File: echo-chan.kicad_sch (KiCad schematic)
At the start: 50 parts, among them J1 SJ1-3533NS, J2 USB_B, SW1 SW_Push, T1 Transformer_1P_1S, U1 JAMMA, U2 JAMMA, U3 AT90USB1286, U4 HD15, U6 THS7374, Y1 16MHz

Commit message: [SCHEMATIC] assign footprints to symbols
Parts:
- C11, C3, C8: footprint (none) -> Capacitor_SMD:C_0805_2012Metric
- C15, C17, C19, C21: footprint (none) -> Capacitor_THT:CP_Radial_D8.0mm_P3.50mm
- J2: footprint footprints:USB_B_OST_USB-B1HSxx_Horizontal -> Connector_USB:USB_B_OST_USB-B1HSxx_Horizontal
- R1, R10, R11, R12, R13, R14, R15, R16, R17, R2, R3, R4, R40, R5, R6, R7, R8, R9: footprint footprints:R_0805_2012Metric -> Resistor_SMD:R_0805_2012Metric
- SW1: footprint footprints:BUTTON -> Button_Switch_THT:SW_PUSH_6mm
- U3: footprint footprints:TQFP-64_14x14mm_P0.8mm -> Package_QFP:TQFP-64_14x14mm_P0.8mm
- U4: footprint footprints:DSUB-15-HD_Female_Horizontal_P2.29x2.54mm_EdgePinOffset9.40mm -> Connector_Dsub:DSUB-15-HD_Female_Horizontal_P2.29x2.54mm_EdgePinOffset9.40mm
- Y1: footprint footprints:Crystal_SMD_SeikoEpson_FA238-4Pin_3.2x2.5mm -> Crystal:Crystal_HC49-4H_Vertical
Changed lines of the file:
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@@
 			)
 		)
-		(property "Footprint" "footprints:TQFP-64_14x14mm_P0.8mm"
+		(property "Footprint" "Package_QFP:TQFP-64_14x14mm_P0.8mm"
 			(at 209.55 69.85 0)
 			(effects
@@
 			)
 		)
-		(property "Footprint" "footprints:R_0805_2012Metric"
+		(property "Footprint" "Resistor_SMD:R_0805_2012Metric"
 			(at 137.16 106.172 90)
 			(effects
@@
 			)
 		)
-		(property "Footprint" "footprints:R_0805_2012Metric"
+		(property "Footprint" "Resistor_SMD:R_0805_2012Metric"
 			(at 137.16 108.712 90)
 			(effects
@@
 			)
 		)
-		(property "Footprint" "footprints:R_0805_2012Metric"
+		(property "Footprint" "Resistor_SMD:R_0805_2012Metric"
 			(at 269.24 69.342 90)
 			(effects
@@
 			)
 		)
-		(property "Footprint" "footprints:BUTTON"
+		(property "Footprint" "Button_Switch_THT:SW_PUSH_6mm"
 			(at 207.01 120.65 0)
 			(effects
@@
 			)
 		)
-		(property "Footprint" "footprints:Crystal_SMD_SeikoEpson_FA238-4Pin_3.2x2.5mm"
+		(property "Footprint" "Crystal:Crystal_HC49-4H_Vertical"
 			(at 236.22 119.38 0)
 			(effects
@@
 			)
 		)
-		(property "Footprint" "footprints:DSUB-15-HD_Female_Horizontal_P2.29x2.54mm_EdgePinOffset9.40mm"
+		(property "Footprint" "Connector_Dsub:DSUB-15-HD_Female_Horizontal_P2.29x2.54mm_EdgePinOffset9.40mm"
 			(at 128.27 33.02 0)
 			(effects
@@
 			)
 		)
-		(property "Footprint" "footprints:USB_B_OST_USB-B1HSxx_Horizontal"
+		(property "Footprint" "Connector_USB:USB_B_OST_USB-B1HSxx_Horizontal"
 			(at 129.54 109.22 0)
 			(effects
@@
 		(on_board yes)
 		(dnp no)
-		(property "Reference" "#PWR?"
+		(property "Reference" "#PWR0101"
 			(at 240.03 165.1 0)
 			(effects
@@
 			(project "echo-chan"
 				(path "/f9e5ab77-ac00-48f5-910f-38a287c63fee"
-					(reference "#PWR?")
+					(reference "#PWR0101")
 					(unit 1)
 				)
@@
 			)
 		)
-		(property "Footprint" "footprints:R_0805_2012Metric"
+		(property "Footprint" "Resistor_SMD:R_0805_2012Metric"
 			(at 209.55 150.368 90)
 			(effects
@@
 			)
 		)
-		(property "Footprint" "footprints:R_0805_2012Metric"
+		(property "Footprint" "Resistor_SMD:R_0805_2012Metric"
 			(at 209.55 160.528 90)
 			(effects
@@
 			)
 		)
-		(property "Footprint" "footprints:R_0805_2012Metric"
+		(property "Footprint" "Resistor_SMD:R_0805_2012Metric"
 			(at 212.852 153.67 90)
 			(effects
@@
 			)
 		)
-		(property "Footprint" ""
+		(property "Footprint" "Capacitor_THT:CP_Radial_D8.0mm_P3.50mm"
 			(at 120.65 176.53 0)
 			(effects
@@
 			)
 		)
-		(property "Footprint" ""
+		(property "Footprint" "Capacitor_THT:CP_Radial_D8.0mm_P3.50mm"
 			(at 120.65 185.42 0)
 			(effects
@@
 			)
 		)
-		(property "Footprint" ""
+		(property "Footprint" "Capacitor_SMD:C_0805_2012Metric"
 			(at 245.11 115.57 0)
 			(effects
@@
 			)
 		)
-		(property "Footprint" "footprints:R_0805_2012Metric"
+		(property "Footprint" "Resistor_SMD:R_0805_2012Metric"
 			(at 40.64 162.052 90)
 			(effects
@@
 			)
 		)
-		(property "Footprint" ""
+		(property "Footprint" "Capacitor_THT:CP_Radial_D8.0mm_P3.50mm"
 			(at 120.65 158.75 0)
 			(effects
@@
 			)
 		)
-		(property "Footprint" "footprints:R_0805_2012Metric"
+		(property "Footprint" "Resistor_SMD:R_0805_2012Metric"
 			(at 45.212 181.61 90)
 			(effects
@@
 			)
 		)
-		(property "Footprint" "footprints:R_0805_2012Metric"
+		(property "Footprint" "Resistor_SMD:R_0805_2012Metric"
 			(at 57.912 181.61 90)
 			(effects
@@
 			)
 		)
-		(property "Footprint" ""
+		(property "Footprint" "Capacitor_SMD:C_0805_2012Metric"
 			(at 184.15 73.66 0)
 			(effects
@@
 			)
 		)
-		(property "Footprint" ""
+		(property "Footprint" "Capacitor_SMD:C_0805_2012Metric"
 			(at 245.11 123.19 0)
 			(effects
@@
 			)
 		)
-		(property "Footprint" "footprints:R_0805_2012Metric"
+		(property "Footprint" "Resistor_SMD:R_0805_2012Metric"
 			(at 104.14 169.672 90)
 			(effects
@@
 			)
 		)
-		(property "Footprint" "footprints:R_0805_2012Metric"
+		(property "Footprint" "Resistor_SMD:R_0805_2012Metric"
 			(at 104.14 162.052 90)
 			(effects
@@
 			)
 		)
-		(property "Footprint" "footprints:R_0805_2012Metric"
+		(property "Footprint" "Resistor_SMD:R_0805_2012Metric"
 			(at 40.64 164.592 90)
 			(effects
@@
 			)
 		)
-		(property "Footprint" ""
+		(property "Footprint" "Capacitor_THT:CP_Radial_D8.0mm_P3.50mm"
 			(at 120.65 167.64 0)
 			(effects
@@
 			)
 		)
-		(property "Footprint" "footprints:R_0805_2012Metric"
+		(property "Footprint" "Resistor_SMD:R_0805_2012Metric"
 			(at 40.64 169.672 90)
 			(effects
@@
 			)
 		)
-		(property "Footprint" "footprints:R_0805_2012Metric"
+		(property "Footprint" "Resistor_SMD:R_0805_2012Metric"
 			(at 40.64 167.132 90)
 			(effects
@@
 			)
 		)
-		(property "Footprint" "footprints:R_0805_2012Metric"
+		(property "Footprint" "Resistor_SMD:R_0805_2012Metric"
 			(at 64.262 181.61 90)
 			(effects
@@
 			)
 		)
-		(property "Footprint" "footprints:R_0805_2012Metric"
+		(property "Footprint" "Resistor_SMD:R_0805_2012Metric"
 			(at 104.14 167.132 90)
 			(effects
@@
 			)
 		)
-		(property "Footprint" "footprints:R_0805_2012Metric"
+		(property "Footprint" "Resistor_SMD:R_0805_2012Metric"
 			(at 51.562 181.61 90)
 			(effects
@@
 			)
 		)
-		(property "Footprint" "footprints:R_0805_2012Metric"
+		(property "Footprint" "Resistor_SMD:R_0805_2012Metric"
 			(at 104.14 164.592 90)
 			(effects

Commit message: [SCHEMATIC] Change +5V to VBUS for MCU
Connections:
- net +5V: no longer C1.1, C2.1, C4.1, C7.1, C9.2, J2.1 (VBUS), U3.21 (VCC), U3.3 (UVcc), U3.52 (VCC), U3.64 (AVCC), U3.8 (VBus)
- new net VBUS: C1.1, C2.1, C4.1, C7.1, C9.2, J2.1 (VBUS), U3.21 (VCC), U3.3 (UVcc), U3.52 (VCC), U3.64 (AVCC), U3.8 (VBus)
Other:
- moved on the sheet: C2, C5, C7, C9

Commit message: [SCHEMATIC] Fix typos in schematic block labels
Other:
- note added: "AUDIO OUT"
- note added: "MICROCONTROLLER"
- note removed: "AUDIO TRANSFORMER"
- note removed: "MICRCONTROLLER"
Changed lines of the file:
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@@
 		)
 	)
-	(text "MICRCONTROLLER"
+	(text "MICROCONTROLLER"
 		(exclude_from_sim no)
 		(at 226.06 15.748 0)
@@
 		)
 	)
-	(text "AUDIO TRANSFORMER"
+	(text "AUDIO OUT"
 		(exclude_from_sim no)
 		(at 227.076 139.7 0)

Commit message: [SCHEMATIC] Fix inverted U2 JAMMA edge
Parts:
- U4: footprint Connector_Dsub:DSUB-15-HD_Female_Horizontal_P2.29x2.54mm_EdgePinOffset9.40mm -> echo-chan:DSUB-15-HD_Female_Horizontal_P2.29x2.54mm_EdgePinOffset9.40mm_anchors
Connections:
- net +12V: now also U2.6 (+12V), U2.F (+12V); no longer U2.23 (P1_BUTTON_2), U2.a (P2_BUTTON_2)
- net +5V: now also U2.3 (+5V), U2.4 (+5V), U2.C (+5V), U2.D (+5V); no longer U2.25 (P1_BUTTON_4), U2.26 (P1_BUTTON_5), U2.c (P2_BUTTON_4), U2.d (P2_BUTTON_5)
- net -5V: now also U2.5 (-5V), U2.E (-5V); no longer U2.24 (P1_BUTTON_3), U2.b (P2_BUTTON_3)
- net COIN_1: now also U2.16 (COIN_1); no longer U2.P (VIDEO_SYNC)
- net COIN_2: now also U2.T (COIN_2); no longer U2.13 (VIDEO_BLUE)
- net COIN_COUNT_1: now also U2.8 (COIN_COUNTER_1); no longer U2.Y (P2_RIGHT)
- net COIN_COUNT_2: now also U2.J (COIN_COUNTER_2); no longer U2.21 (P1_RIGHT)
- net COIN_LOCK_1: now also U2.9 (COIN_LOCKOUT_1); no longer U2.X (P2_LEFT)
- net COIN_LOCK_2: now also U2.K (COIN_LOCKOUT_2); no longer U2.20 (P1_LEFT)
- net P1_B1: now also U2.22 (P1_BUTTON_1); no longer U2.H (KEY)
- net P1_B2: now also U2.23 (P1_BUTTON_2); no longer U2.F (+12V)
- net P1_B3: now also U2.24 (P1_BUTTON_3); no longer U2.E (-5V)
- net P1_B4: now also U2.25 (P1_BUTTON_4); no longer U2.D (+5V)
- net P1_B5: now also U2.26 (P1_BUTTON_5); no longer U2.C (+5V)
- net P1_DOWN: now also U2.19 (P1_DOWN); no longer U2.L (SPEAKER(-))
- net P1_LEFT: now also U2.20 (P1_LEFT); no longer U2.K (COIN_LOCKOUT_2)
- net P1_RIGHT: now also U2.21 (P1_RIGHT); no longer U2.J (COIN_COUNTER_2)
- net P1_START: now also U2.17 (P1_START); no longer U2.N (VIDEO_GREEN)
- net P1_UP: now also U2.18 (P1_UP); no longer U2.M (NC)
- net P2_B1: now also U2.Z (P2_BUTTON_1); no longer U2.7 (KEY)
- net P2_B2: now also U2.a (P2_BUTTON_2); no longer U2.6 (+12V)
- net P2_B3: now also U2.b (P2_BUTTON_3); no longer U2.5 (-5V)
- net P2_B4: now also U2.c (P2_BUTTON_4); no longer U2.4 (+5V)
- net P2_B5: now also U2.d (P2_BUTTON_5); no longer U2.3 (+5V)
- net P2_DOWN: now also U2.W (P2_DOWN); no longer U2.10 (SPEAKER(+))
- net P2_LEFT: now also U2.X (P2_LEFT); no longer U2.9 (COIN_LOCKOUT_1)
- net P2_RIGHT: now also U2.Y (P2_RIGHT); no longer U2.8 (COIN_COUNTER_1)
- net P2_START: now also U2.U (P2_START); no longer U2.12 (VIDEO_RED)
- net P2_UP: now also U2.V (P2_UP); no longer U2.11 (NC)
- net SERVICE: now also U2.R (SERVICE); no longer U2.15 (TEST)
- net SPEAKER+: now also U2.10 (SPEAKER(+)); no longer U2.W (P2_DOWN)
- net SPEAKER-: now also U2.L (SPEAKER(-)); no longer U2.19 (P1_DOWN)
- net TEST: now also U2.15 (TEST); no longer U2.R (SERVICE)
- net TILT: now also U2.S (TILT); no longer U2.14 (VIDEO_GND)
- net VIDEO_BLUE: now also U2.13 (VIDEO_BLUE); no longer U2.T (COIN_2)
- net VIDEO_GND: now also U2.14 (VIDEO_GND); no longer U2.S (TILT)
- net VIDEO_GREEN: now also U2.N (VIDEO_GREEN); no longer U2.17 (P1_START)
- net VIDEO_RED: now also U2.12 (VIDEO_RED); no longer U2.U (P2_START)
- net VIDEO_SYNC: now also U2.P (VIDEO_SYNC); no longer U2.16 (COIN_1)
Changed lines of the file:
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@@
 	)
 	(junction
+		(at 73.66 27.94)
+		(diameter 0)
+		(color 0 0 0 0)
+	)
+	(junction
 		(at 214.63 148.59)
 		(diameter 0)
@@
 	)
 	(junction
-		(at 73.66 27.94)
-		(diameter 0)
-		(color 0 0 0 0)
-	)
-	(junction
 		(at 39.37 29.21)
 		(diameter 0)
@@
 	(symbol
 		(lib_id "jamma-streamer-rescue:JAMMA-jamma-streamer-rescue")
-		(at 66.04 63.5 270)
-		(mirror x)
+		(at 66.04 62.23 270)
 		(unit 1)
 		(exclude_from_sim no)
@@
 		(dnp no)
 		(property "Reference" "U2"
-			(at 58.42 63.5 0)
+			(at 63.754 25.4 90)
 			(effects
 				(font
@@
 		)
 		(property "Value" "JAMMA"
-			(at 60.96 63.5 0)
+			(at 60.96 62.23 0)
 			(effects
 				(font
@@
 		)
 		(property "Footprint" "footprints:JAMMA"
-			(at 63.5 71.12 0)
+			(at 63.5 54.61 0)
 			(effects
 				(font
@@
 		)
 		(property "Datasheet" ""
-			(at 63.5 71.12 0)
+			(at 63.5 54.61 0)
 			(effects
 				(font
@@
 		)
 		(property "Description" ""
-			(at 66.04 63.5 0)
+			(at 66.04 62.23 0)
 			(effects
 				(font
@@
 		(dnp no)
 		(property "Reference" "U1"
-			(at 24.13 62.23 0)
+			(at 29.718 25.4 90)
 			(effects
 				(font
@@
 			)
 		)
-		(property "Footprint" "Connector_Dsub:DSUB-15-HD_Female_Horizontal_P2.29x2.54mm_EdgePinOffset9.40mm"
+		(property "Footprint" "echo-chan:DSUB-15-HD_Female_Horizontal_P2.29x2.54mm_EdgePinOffset9.40mm_anchors"
 			(at 128.27 33.02 0)
 			(effects

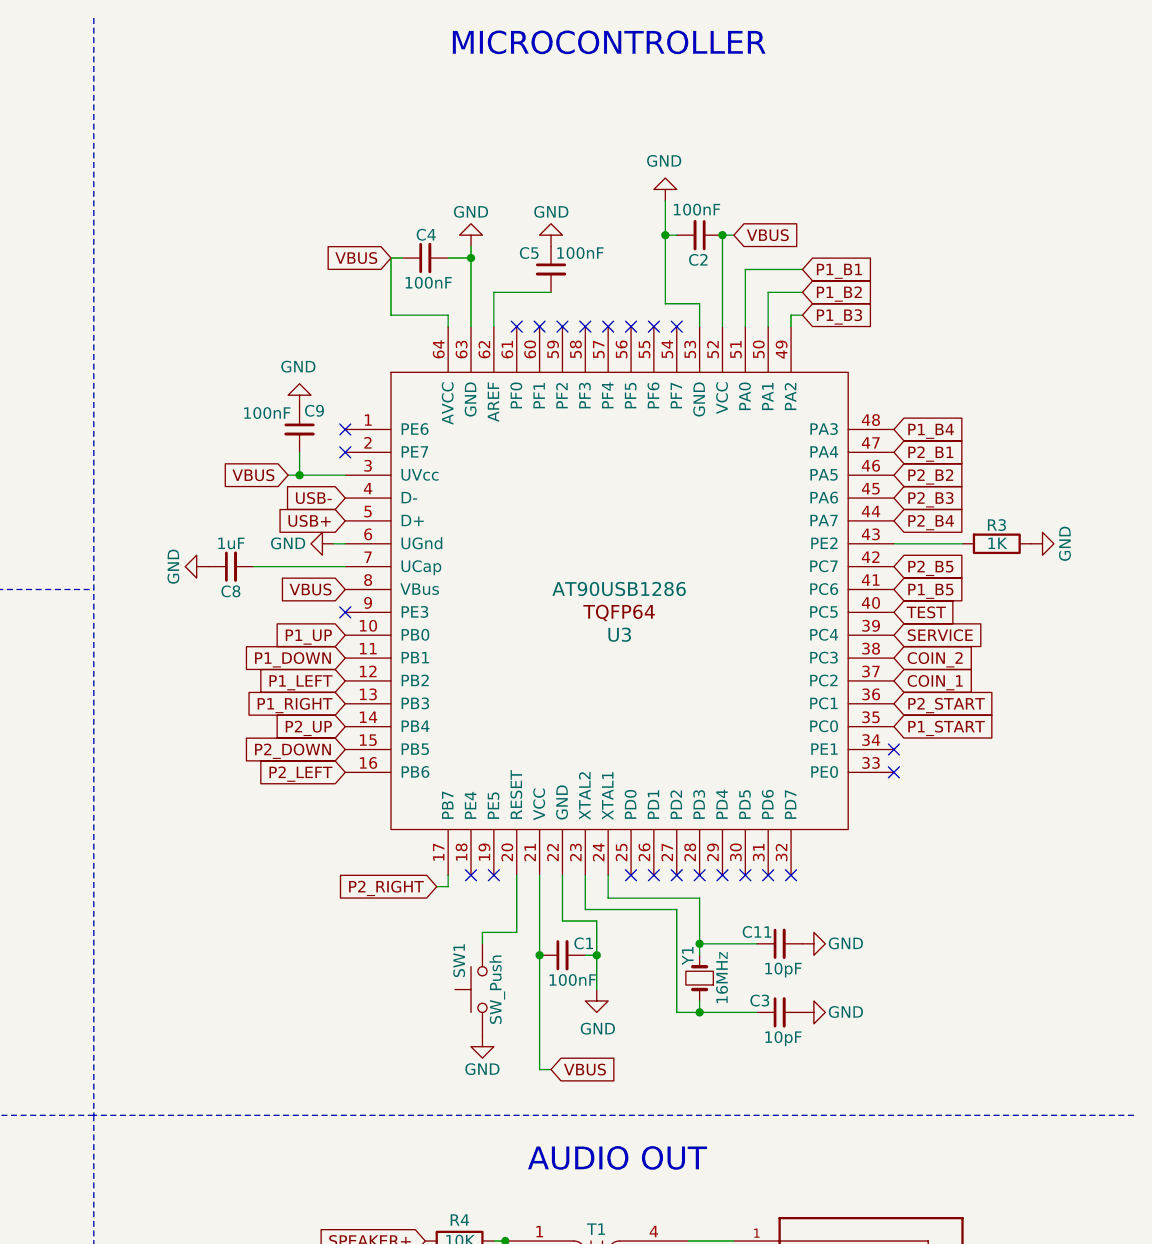
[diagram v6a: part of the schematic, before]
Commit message: [SCHEMATIC] MCU refactor
- Remove test/service connections
- Move all button inputs to 2 sides to simplify routing
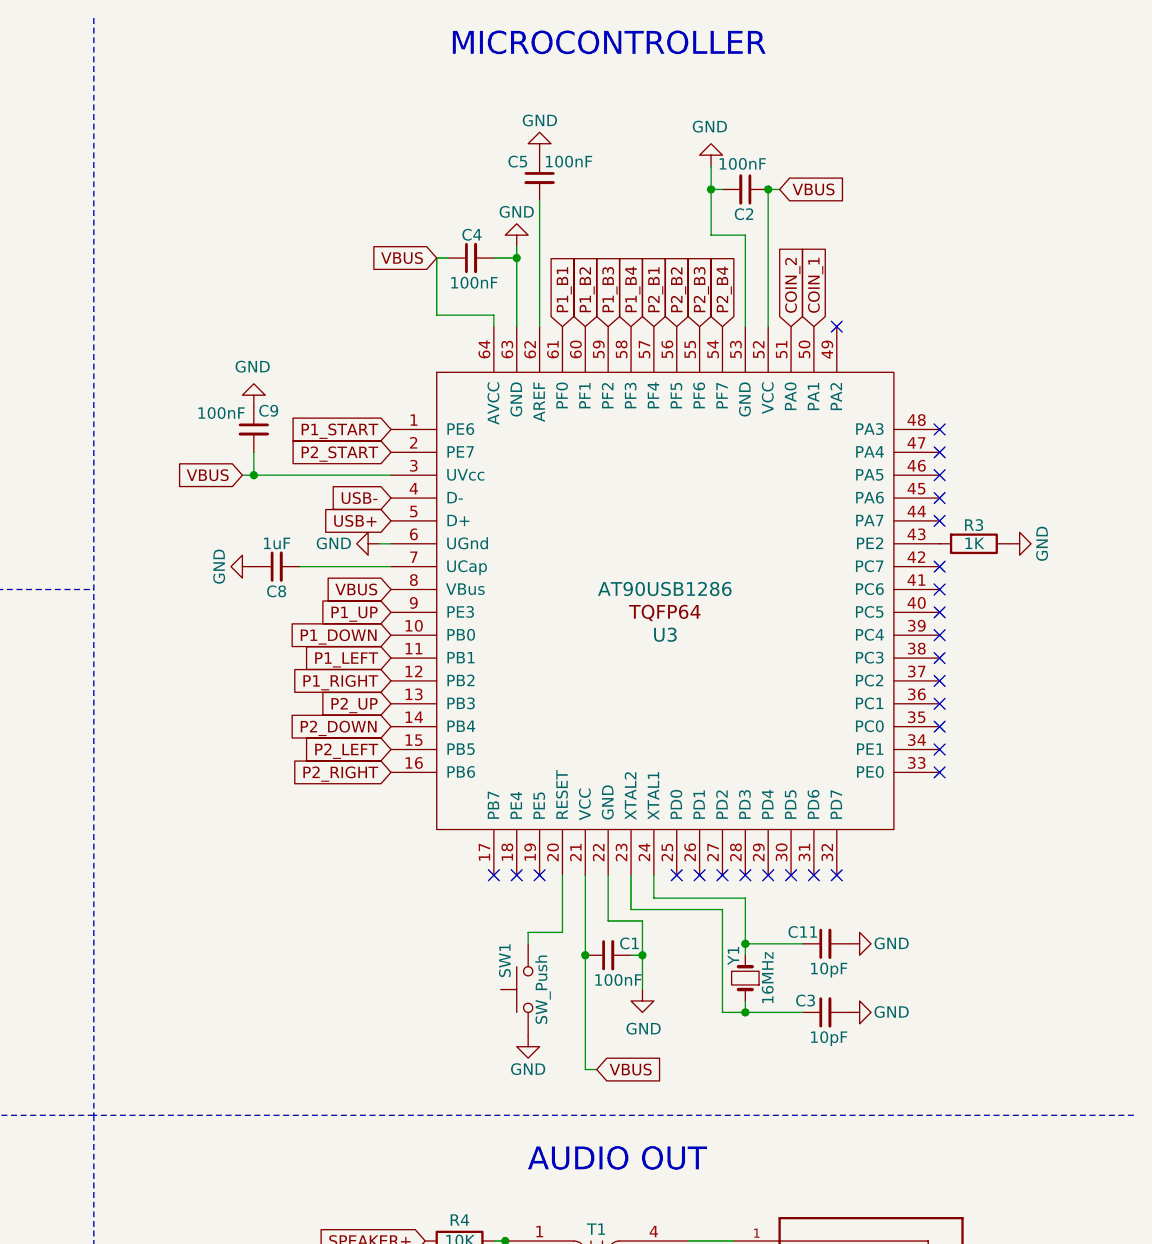
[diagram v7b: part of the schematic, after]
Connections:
- net COIN_1: now also U3.50 (PA1); no longer U3.37 (PC2)
- net COIN_2: now also U3.51 (PA0); no longer U3.38 (PC3)
- net P1_B1: now also U3.61 (PF0); no longer U3.51 (PA0)
- net P1_B2: now also U3.60 (PF1); no longer U3.50 (PA1)
- net P1_B3: now also U3.59 (PF2); no longer U3.49 (PA2)
- net P1_B4: now also U3.58 (PF3); no longer U3.48 (PA3)
- net P1_B5: no longer U3.41 (PC6)
- net P1_DOWN: now also U3.10 (PB0); no longer U3.11 (PB1)
- net P1_LEFT: now also U3.11 (PB1); no longer U3.12 (PB2)
- net P1_RIGHT: now also U3.12 (PB2); no longer U3.13 (PB3)
- net P1_START: now also U3.1 (PE6); no longer U3.35 (PC0)
- net P1_UP: now also U3.9 (PE3); no longer U3.10 (PB0)
- net P2_B1: now also U3.57 (PF4); no longer U3.47 (PA4)
- net P2_B2: now also U3.56 (PF5); no longer U3.46 (PA5)
- net P2_B3: now also U3.55 (PF6); no longer U3.45 (PA6)
- net P2_B4: now also U3.54 (PF7); no longer U3.44 (PA7)
- net P2_B5: no longer U3.42 (PC7)
- net P2_DOWN: now also U3.14 (PB4); no longer U3.15 (PB5)
- net P2_LEFT: now also U3.15 (PB5); no longer U3.16 (PB6)
- net P2_RIGHT: now also U3.16 (PB6); no longer U3.17 (PB7)
- net P2_START: now also U3.2 (PE7); no longer U3.36 (PC1)
- net P2_UP: now also U3.13 (PB3); no longer U3.14 (PB4)
- net SERVICE: no longer U3.39 (PC4)
- net TEST: no longer U3.40 (PC5)
- no-connect marks 36 -> 40
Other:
- moved on the sheet: C1, C11, C2, C3, C4, C5, C8, C9, R3, SW1, U3, Y1
